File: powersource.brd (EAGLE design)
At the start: 93.1 x 70.2 mm, 11 parts

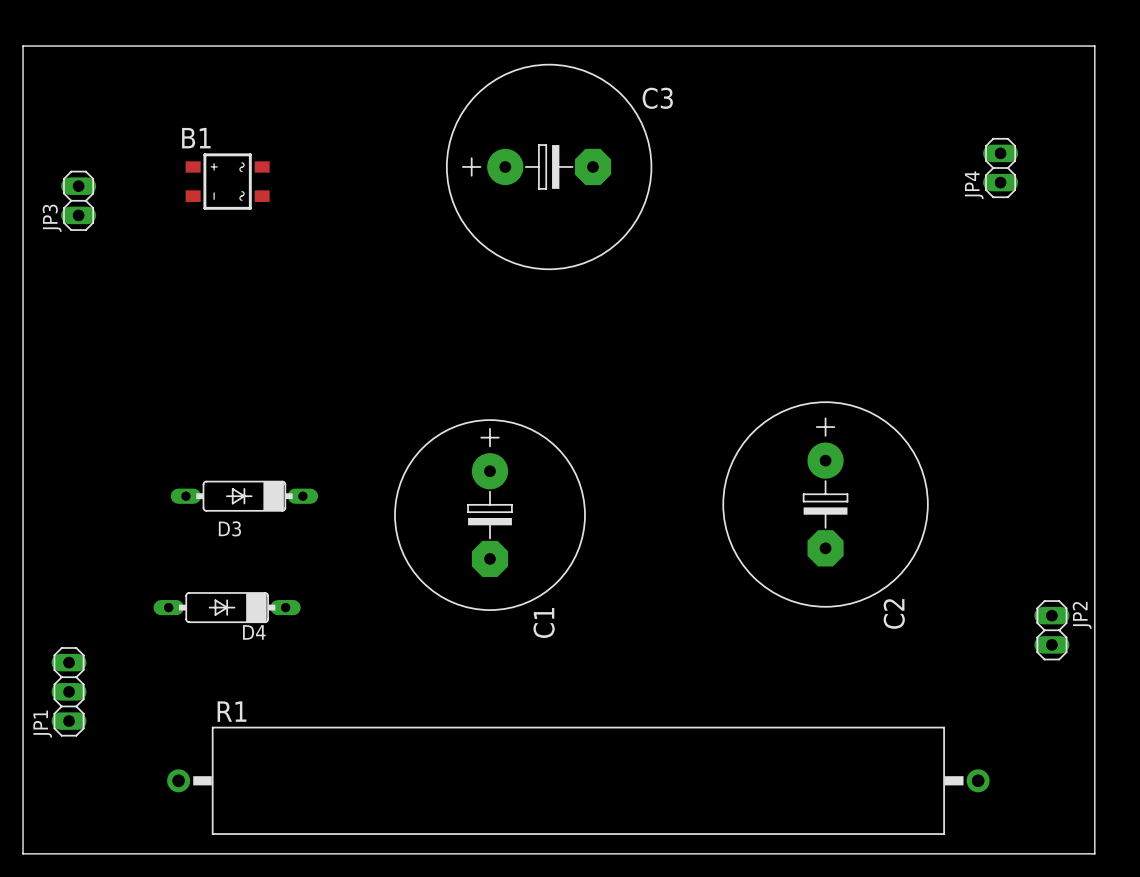
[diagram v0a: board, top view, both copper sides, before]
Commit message: [add]電源回路をいい感じにした
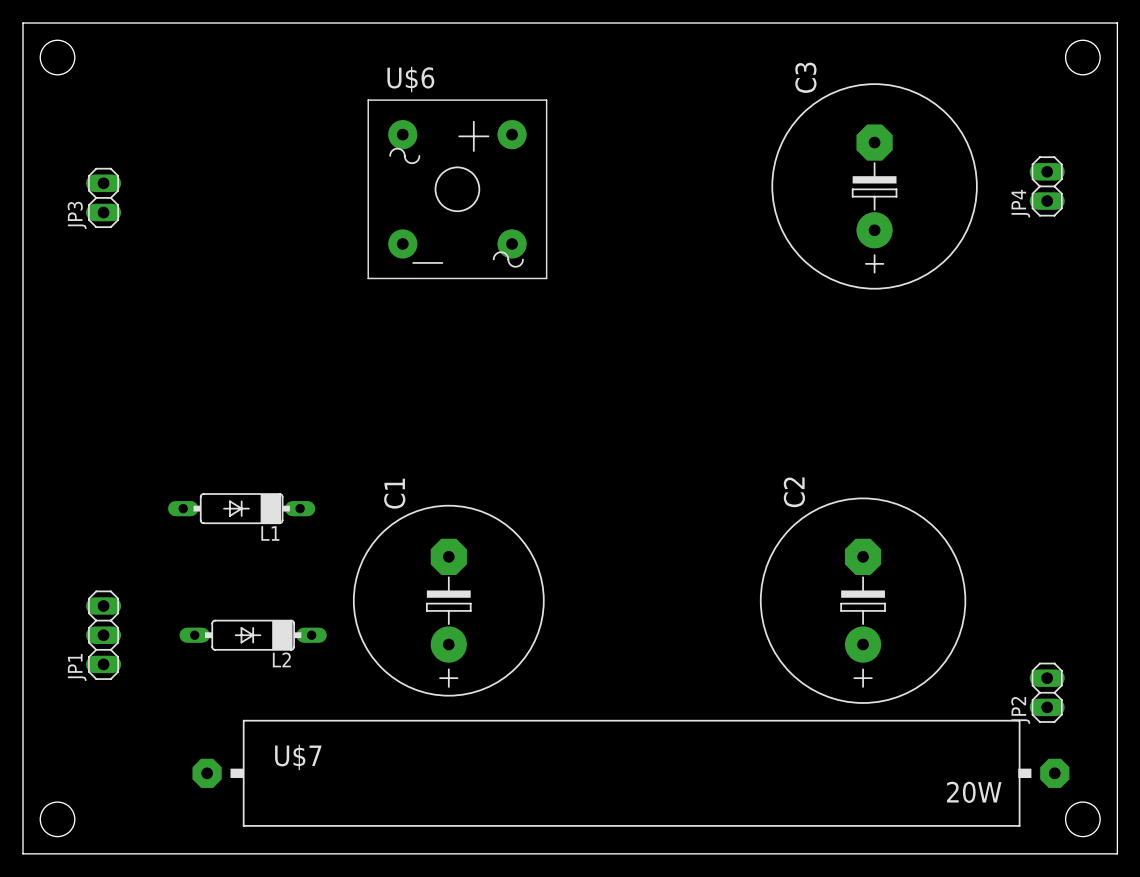
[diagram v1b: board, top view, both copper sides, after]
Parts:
- removed B1: B1S, rectifier:MBS
- removed D3, D4: (no value), diode:DO07
- removed R1: (no value), resistor-power:RWM10X65
- added L1, L2: DIODE, VacuumTube:DO07
- added U$6: BRIDGERECTIFIER, VacuumTube:BRIDGERECTIFIER
- added U$7: RESISTOR, VacuumTube:RESISTOR
- C1: value (none) -> E7.5-16; device rcl:E7,5-16 -> VacuumTube:E7,5-16
- C2, C3: value (none) -> E7.5-18; device rcl:E7,5-18 -> VacuumTube:E7,5-18
- JP1: device pinhead:1X03 -> VacuumTube:1X03
- JP2, JP3, JP4: device pinhead:1X02 -> VacuumTube:1X02
- moved C3 28.3 mm to (74.0, 58.0), turned to 90 degrees
- moved C2 8.97 mm to (73.0, 22.0), turned to 90 degrees
- moved C1 8.26 mm to (37.0, 22.0), turned to 90 degrees
- moved JP1 5.76 mm to (7.00, 19.0)
- moved JP2 5.45 mm to (89.0, 14.0), turned to 90 degrees
- moved JP4 4.35 mm to (89.0, 58.0)
- moved JP3 2.18 mm to (7.00, 57.0)
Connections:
- removed net N$5: B1.AC1, JP3.2
- new net N$1: JP1.2, L2.A
- net GND: now also U$6.AC2; no longer B1.-
- net N$14: now also U$7.2; no longer R1.2
- net N$15: now also L1.C, L2.C, U$7.1; no longer D3.C, D4.C, R1.1
- net N$2: now also L1.A; no longer D3.A
- net N$3: now also JP3.2, U$6.-; no longer D4.A, JP1.2
- net N$4: now also U$6.+; no longer B1.AC2
- net N$7: now also U$6.AC1; no longer B1.+
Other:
- board size 93.1 x 70.2 mm -> 95.1 x 72.2 mm

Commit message: [fix]超超微調整
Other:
- board size 95.1 x 72.2 mm -> 95 x 72 mm
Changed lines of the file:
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@@
 </layers>
 <board>
-<fusionsync huburn="a.cGVyc29uYWw6dWUyZDlmMDVj" projecturn="a.cGVyc29uYWw6dWUyZDlmMDVjIzIwMTgxMjMwMTY3NjU5OTU2" f3durn="urn:adsk.wipprod:dm.lineage:1p4ZNr76QF6s9D04_b7MiQ" pcbguid="6f970ecf-14a9-49a9-a88c-6c1ebdaac8da" lastpulledtime="" lastsyncedchangeguid="05b6d938-cdf6-f8e0-c3d8-3ea724515d47"/>
+<fusionsync huburn="a.cGVyc29uYWw6dWUyZDlmMDVj" projecturn="a.cGVyc29uYWw6dWUyZDlmMDVjIzIwMTgxMjMwMTY3NjU5OTU2" f3durn="urn:adsk.wipprod:dm.lineage:1p4ZNr76QF6s9D04_b7MiQ" pcbguid="6f970ecf-14a9-49a9-a88c-6c1ebdaac8da" lastpulledtime="" lastsyncedchangeguid="dffcab59-db55-236d-5594-2eaaafb1d0d9"/>
 <plain>
-<wire x1="0" y1="0" x2="95.1" y2="0" width="0" layer="20"/>
-<wire x1="95.1" y1="0" x2="95.1" y2="72.2" width="0" layer="20"/>
-<wire x1="95.1" y1="72.2" x2="0" y2="72.2" width="0" layer="20"/>
-<wire x1="0" y1="72.2" x2="0" y2="0" width="0" layer="20"/>
-<hole x="3" y="3" drill="3"/>
-<hole x="92.1" y="3" drill="3"/>
-<hole x="3" y="69.2" drill="3"/>
-<hole x="92.1" y="69.2" drill="3"/>
+<wire x1="0" y1="0" x2="95" y2="0" width="0" layer="20"/>
+<wire x1="95" y1="0" x2="95" y2="72" width="0" layer="20"/>
+<wire x1="95" y1="72" x2="0" y2="72" width="0" layer="20"/>
+<wire x1="0" y1="72" x2="0" y2="0" width="0" layer="20"/>
+<hole x="3" y="3" drill="3.2"/>
+<hole x="92" y="3" drill="3.2"/>
+<hole x="3" y="69" drill="3.2"/>
+<hole x="92" y="69" drill="3.2"/>
 </plain>
 <attributes>
@@
 <attribute name="VALUE" x="92.175" y="55.46" size="1.27" layer="27" rot="R90"/>
 </element>
-<element name="C1" library="VacuumTube" library_urn="urn:adsk.eagle:library:8044196" package="E7,5-16" package3d_urn="urn:adsk.eagle:package:8399792/1" value="E7.5-16" x="37" y="22" smashed="yes" rot="R90">
+<element name="C1" library="VacuumTube" library_urn="urn:adsk.eagle:library:8044196" package="E7,5-16" package3d_urn="urn:adsk.eagle:package:8399792/3" value="E7.5-16" x="37" y="22" smashed="yes" rot="R90">
 <attribute name="NAME" x="33.19" y="29.874" size="1.778" layer="25" ratio="10" rot="R90"/>
 <attribute name="VALUE" x="41.2926" y="16.92" size="1.778" layer="27" ratio="10" rot="R90"/>
 </element>
-<element name="C2" library="VacuumTube" library_urn="urn:adsk.eagle:library:8044196" package="E7,5-18" package3d_urn="urn:adsk.eagle:package:8399793/1" value="E7.5-18" x="73" y="22" smashed="yes" rot="R90">
+<element name="C2" library="VacuumTube" library_urn="urn:adsk.eagle:library:8044196" package="E7,5-18" package3d_urn="urn:adsk.eagle:package:8399793/3" value="E7.5-18" x="73" y="22" smashed="yes" rot="R90">
 <attribute name="NAME" x="67.92" y="30.001" size="1.778" layer="25" ratio="10" rot="R90"/>
 <attribute name="VALUE" x="77.2926" y="16.92" size="1.778" layer="27" ratio="10" rot="R90"/>
 </element>
-<element name="C3" library="VacuumTube" library_urn="urn:adsk.eagle:library:8044196" package="E7,5-18" package3d_urn="urn:adsk.eagle:package:8399793/1" value="E7.5-18" x="74" y="58" smashed="yes" rot="R90">
+<element name="C3" library="VacuumTube" library_urn="urn:adsk.eagle:library:8044196" package="E7,5-18" package3d_urn="urn:adsk.eagle:package:8399793/3" value="E7.5-18" x="74" y="58" smashed="yes" rot="R90">
 <attribute name="NAME" x="68.92" y="66.001" size="1.778" layer="25" ratio="10" rot="R90"/>
 <attribute name="VALUE" x="78.2926" y="52.92" size="1.778" layer="27" ratio="10" rot="R90"/>
@@
 <attribute name="VALUE" x="34.555" y="52.92" size="1.778" layer="27" ratio="10"/>
 </element>
-<element name="U$7" library="VacuumTube" library_urn="urn:adsk.eagle:library:8044196" package="RESISTOR" package3d_urn="urn:adsk.eagle:package:8399790/1" value="RESISTOR" x="16" y="7" smashed="yes">
+<element name="U$7" library="VacuumTube" library_urn="urn:adsk.eagle:library:8044196" package="RESISTOR" package3d_urn="urn:adsk.eagle:package:8399790/2" value="RESISTOR" x="16" y="7" smashed="yes">
 <attribute name="NAME" x="21.715" y="7.635" size="1.778" layer="25" ratio="10"/>
 <attribute name="VALUE" x="21.715" y="4.46" size="1.778" layer="27" ratio="10"/>
